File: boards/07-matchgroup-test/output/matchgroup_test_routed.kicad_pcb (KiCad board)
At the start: 4 copper layers, 110 x 95 mm, 8 parts, among them J1 FFC6_MIPI, J2 HDMI19, J3 ADDR_HDR, U1 QFN48_DDR_CTRL, U2 QFN48_DRAM, U3 QFN24_MIPI, U4 BGA49_HDMI, U5 QFP48_SRAM

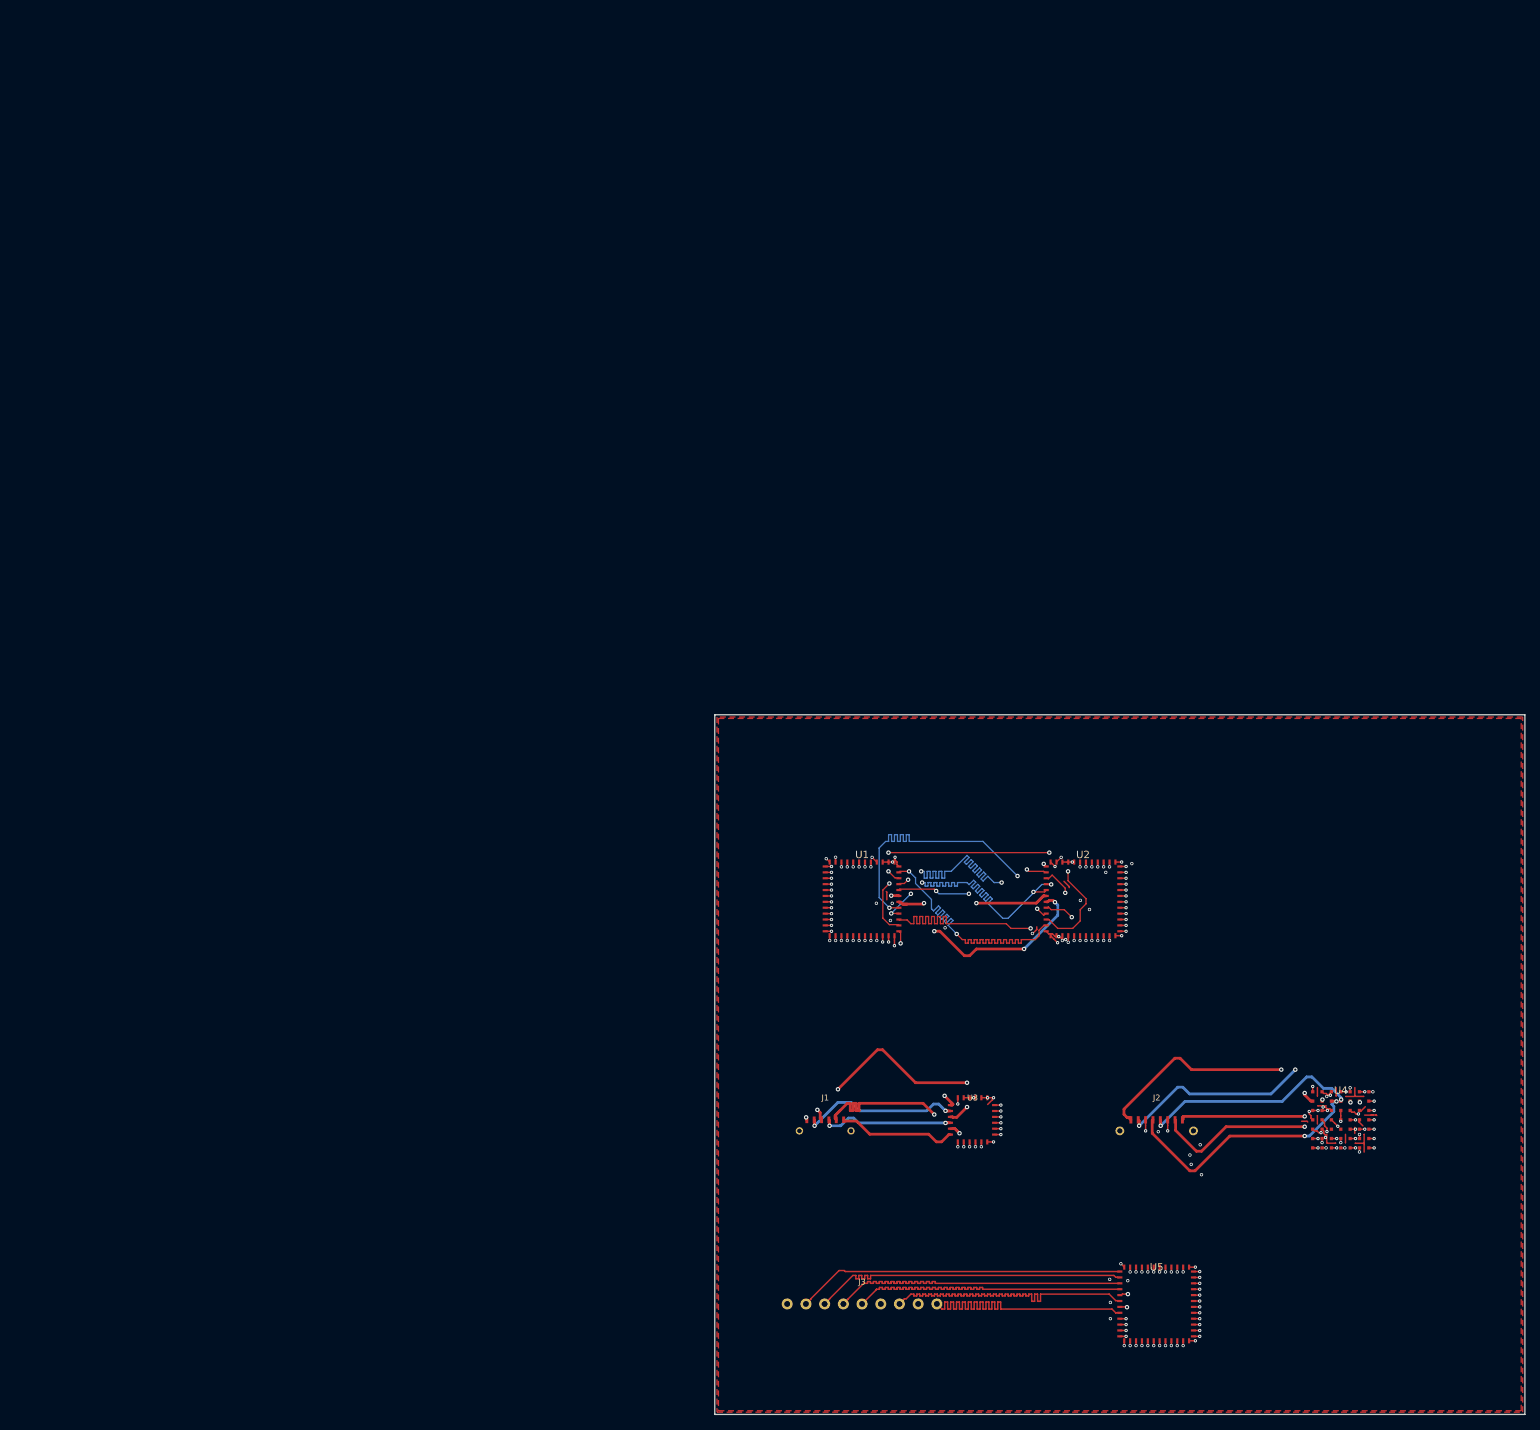
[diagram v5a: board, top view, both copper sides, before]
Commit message: feat(pcb): add page_fit to size sheet to board + center, apply to all boards
Add PCB.page_fit(margin=5.0) which rewrites the (paper ...) node to a tight
(paper "User" W H) sized to the Edge.Cuts bbox plus a uniform margin and
translates every board item (footprints, segments, vias, zones incl.
filled_polygons, gr_* graphics, text) so the board is centered with that
margin. Pure geometric translate — relative geometry, routing and DRC
validity are preserved, no re-route needed.

Expose it as `kct pcb page-fit <pcb> [-o out] [--margin] [--dry-run]` and
wire a PAGE_FIT build step (after stitch, before verify/export) so future
boards are centered too. Apply page_fit to all demo boards (00-07 +
external/softstart), both routed and unrouted PCBs, so the committed
layouts fill + center the KiCanvas viewer instead of sitting tiny in an A4
page. Boards 00/01 stay DRC-clean (0 errors); no board's DRC count changed.

Co-Authored-By: Claude Opus 4.7 <noreply@anthropic.com>
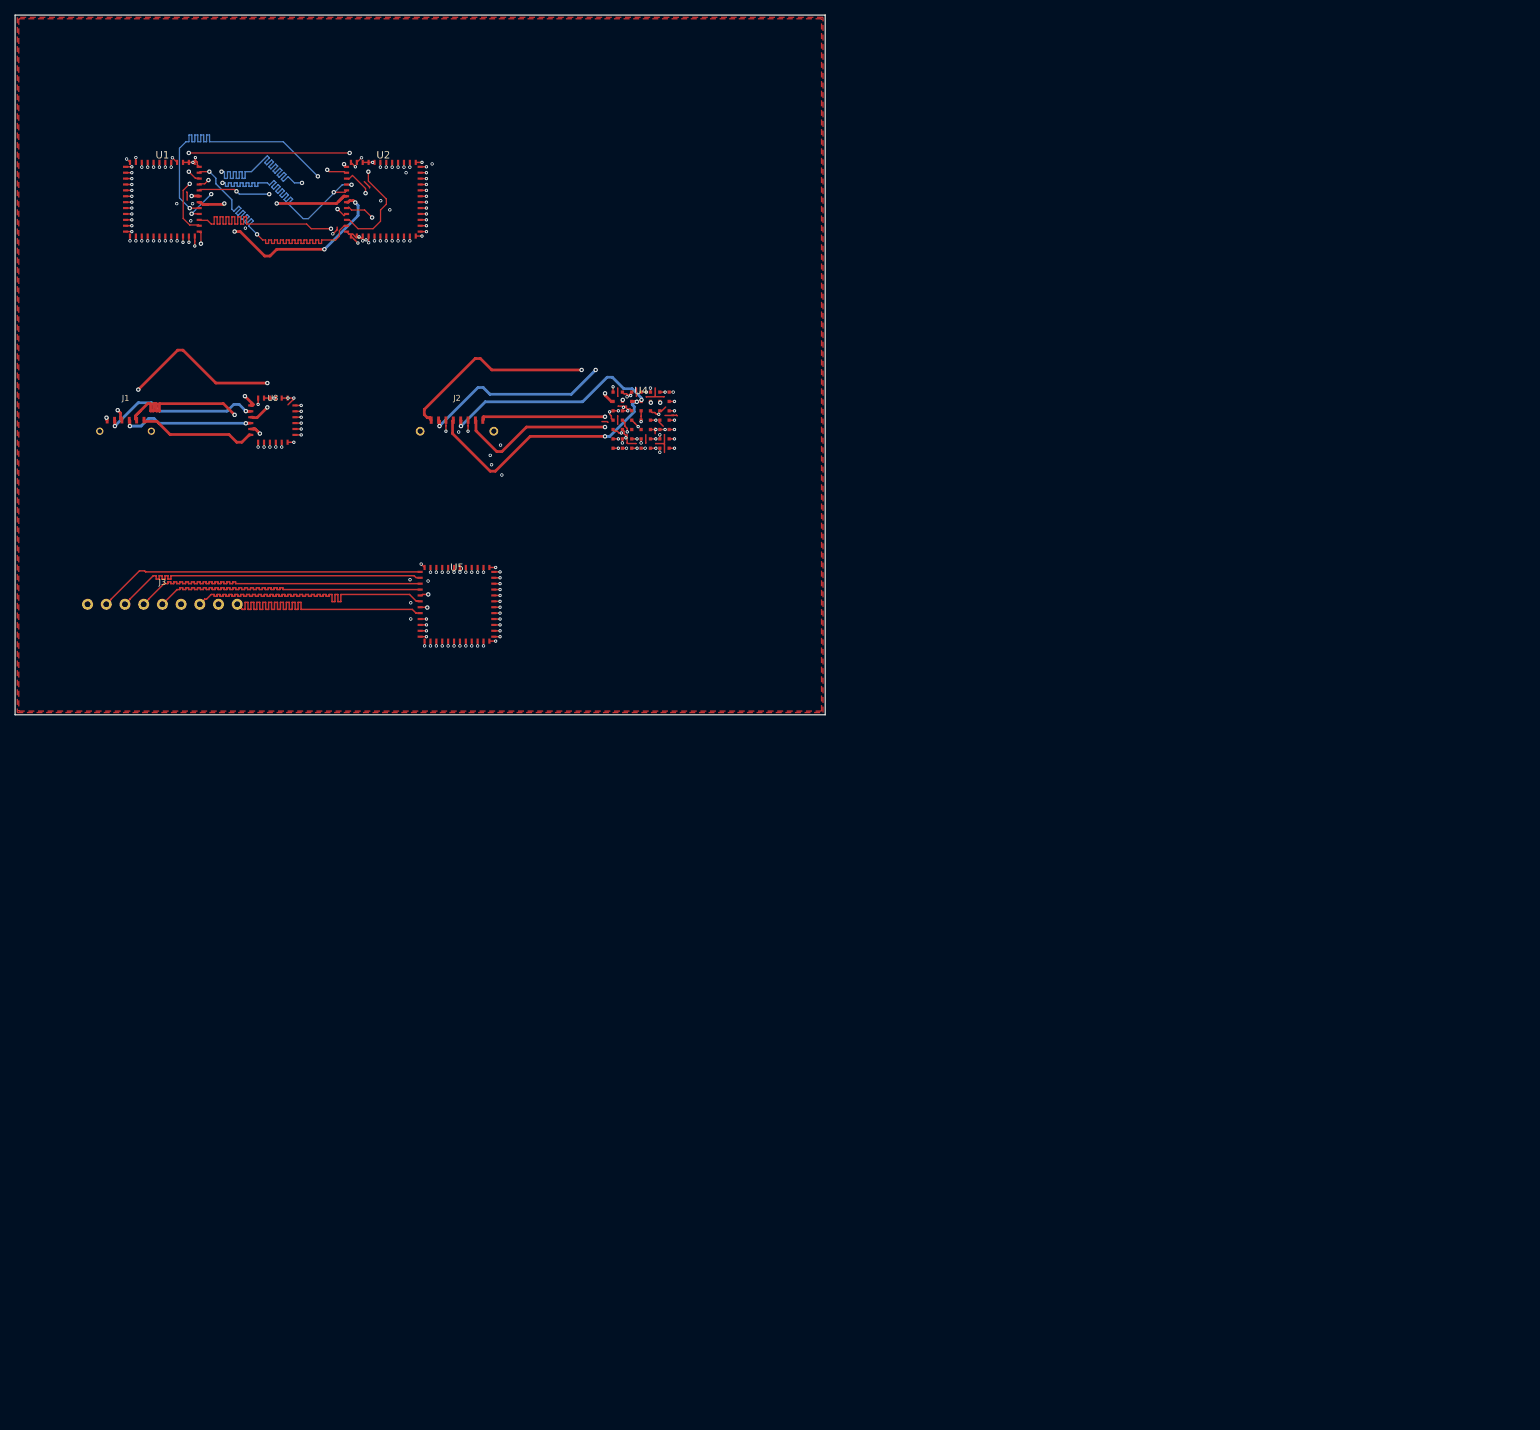
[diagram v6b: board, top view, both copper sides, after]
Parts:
- moved J1 134.4 mm to (20.0, 60.0)
- moved J2 134.4 mm to (65.0, 60.0)
- moved J3 134.4 mm to (25.0, 85.0)
- moved U1 134.4 mm to (25.0, 30.0)
- moved U2 134.4 mm to (55.0, 30.0)
- moved U3 134.4 mm to (40.0, 60.0)
- moved U4 134.4 mm to (90.0, 60.0)
- moved U5 134.4 mm to (65.0, 85.0)
